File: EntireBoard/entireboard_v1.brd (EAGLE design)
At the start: 30 x 30 mm, 48 parts, among them J1 FTSH-105-01-XXX-DV-K, U2 RHD2216_QFN

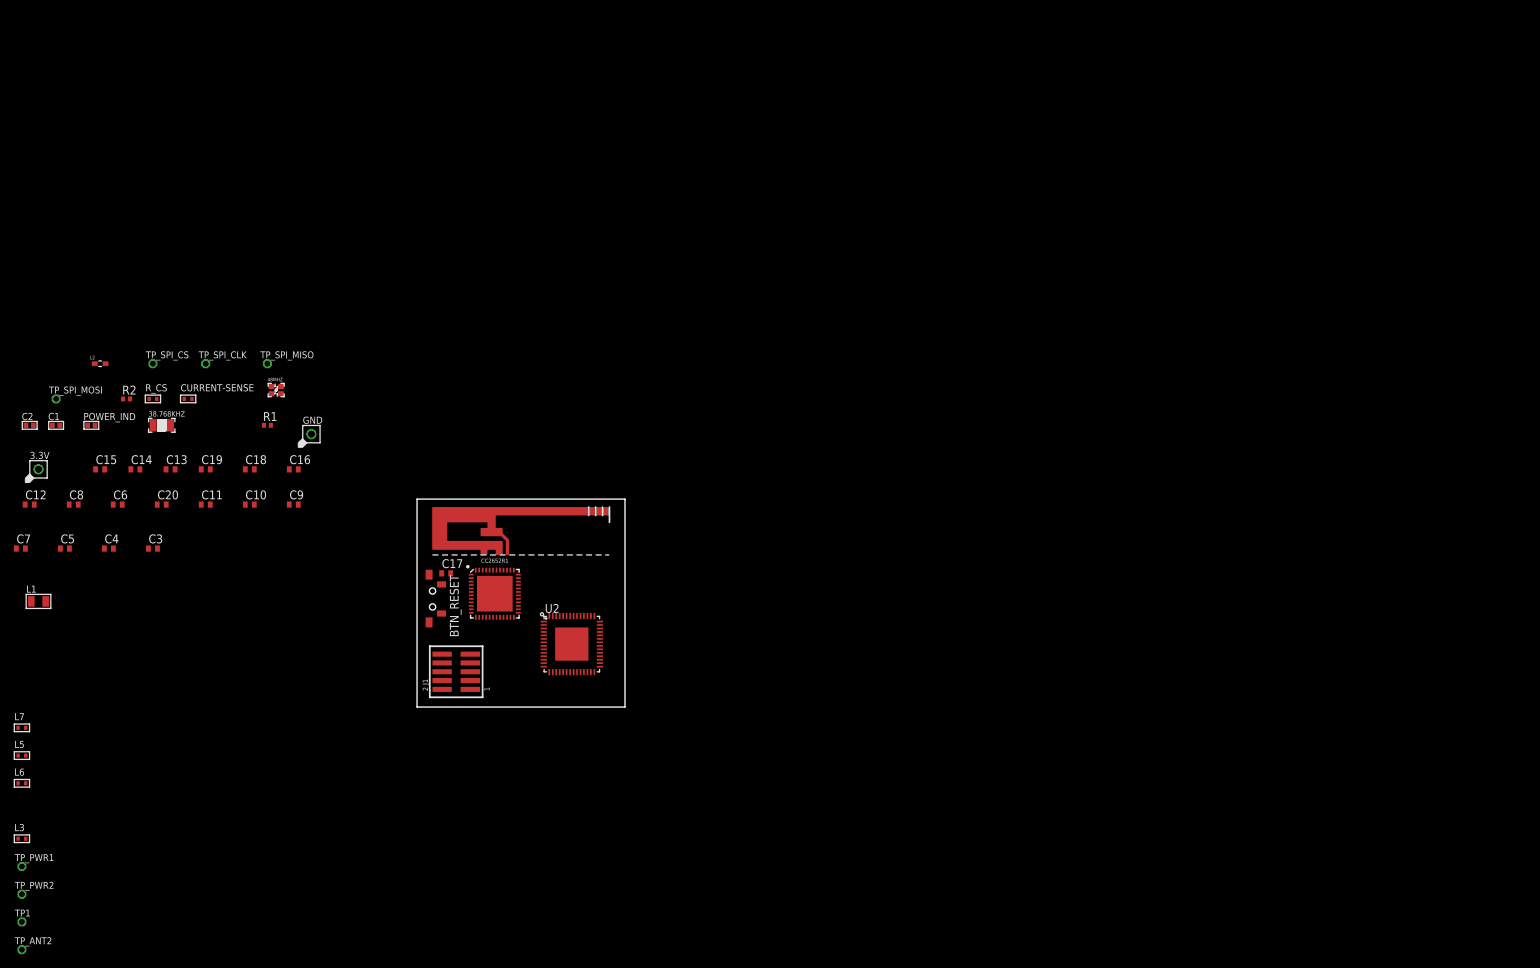
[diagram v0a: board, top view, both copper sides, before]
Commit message: board inconsistencies
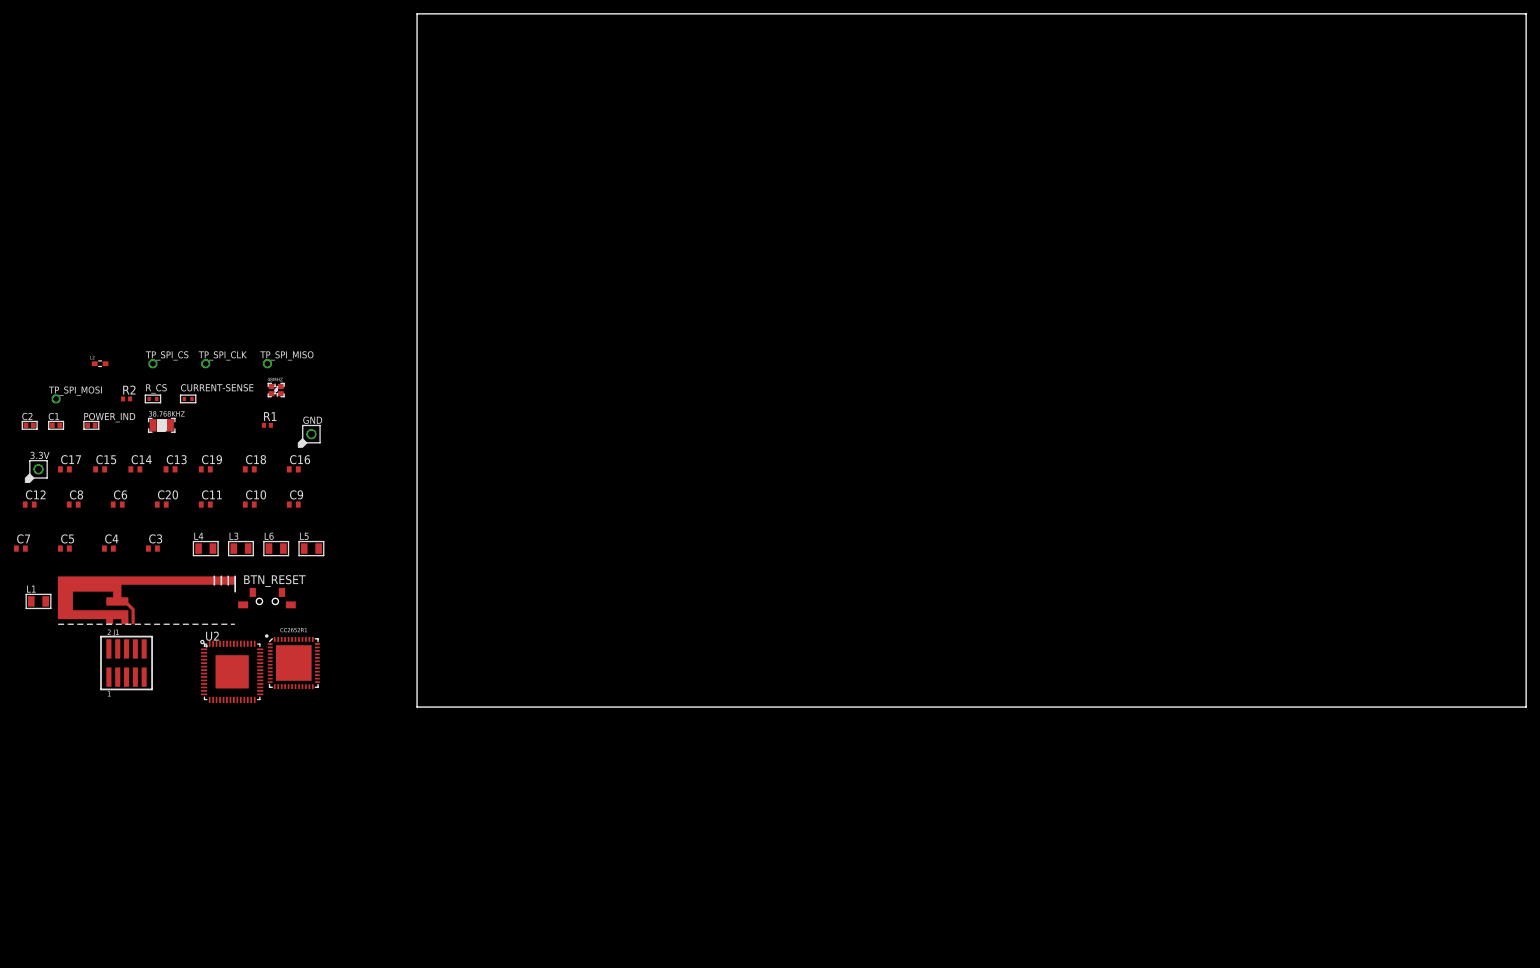
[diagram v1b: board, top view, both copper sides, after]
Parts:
- removed L7: 2.4nH, MF_Passives:L0402
- removed TP1, TP_ANT2, TP_PWR1, TP_PWR2: RHD2000_EVAL_BOARD_TESTPOINT_SMALL, AxonMobile:RHD2000_EVAL_BOARD_TESTPOINT_SMALL
- added L4: 2nH, AxonMobile:RHD2000_EVAL_BOARD_0805
- L3, L5: device MF_Passives:L0402 -> AxonMobile:RHD2000_EVAL_BOARD_0805
- L6: value 2nH -> 2.4nH; device MF_Passives:L0402 -> AxonMobile:RHD2000_EVAL_BOARD_0805
- moved C17 57.0 mm to (-50.8, 34.3)
- moved U$2 54.9 mm to (-43.2, 15.2)
- moved L3 52.4 mm to (-25.4, 22.9)
- moved L5 51.3 mm to (-15.2, 22.9)
- moved L6 49.9 mm to (-20.3, 22.9)
- moved U2 49.2 mm to (-26.7, 5.08)
- moved J1 47.6 mm to (-41.9, 6.35), turned to 0 degrees
- moved CC2652R1 30.7 mm to (-17.8, 6.35)
- moved BTN_RESET 23.8 mm to (-21.6, 15.2), turned to 0 degrees
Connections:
- net N$11: no longer TP1.1
- net N$12: now also L6.2; no longer L7.P$2
- net N$13: no longer TP_PWR2.1
- net N$2: no longer TP_ANT2.1
- net N$7: now also L3.2; no longer L3.P$2
- net N$8: now also L3.1, L4.2; no longer L3.P$1, L6.P$2
- net N$9: now also L4.1, L5.2; no longer L5.P$2, L6.P$1
- net RF_N: now also L5.1; no longer L5.P$1
- net RF_P: now also L6.1; no longer L7.P$1
- net VDDS: no longer TP_PWR1.1
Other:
- board size 30 x 30 mm -> 160 x 100 mm
